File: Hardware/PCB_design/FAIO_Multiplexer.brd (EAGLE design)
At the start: 50.8 x 22.9 mm, 9 parts, among them J1 SJ1-3535NG, J2 SJ1-3535NG, J3 SJ1-3535NG, J4 SJ1-3535NG

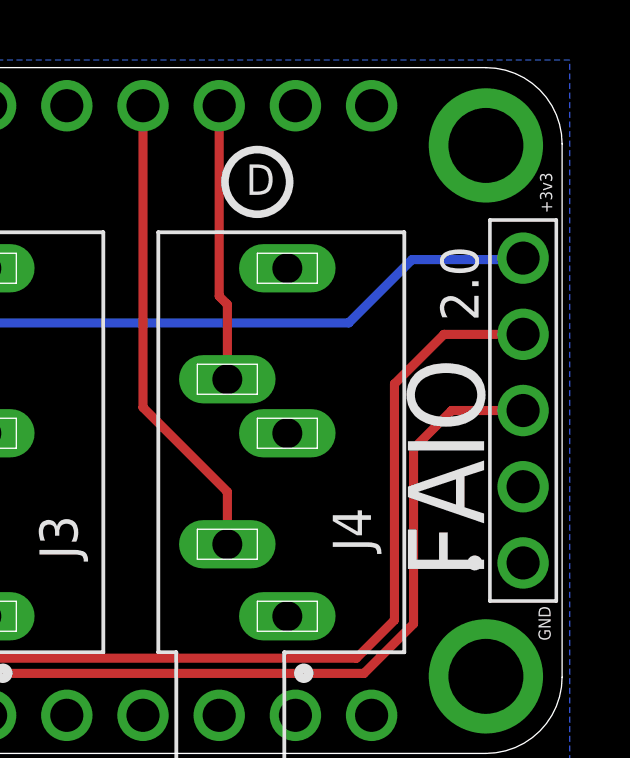
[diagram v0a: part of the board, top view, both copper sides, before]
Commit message: Updated PCB Files: 2.0 text changed to Multiplexer
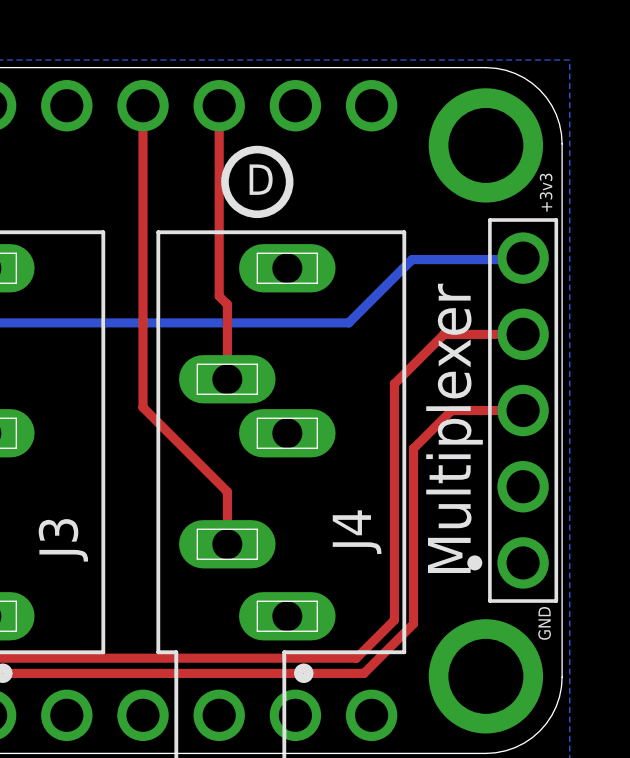
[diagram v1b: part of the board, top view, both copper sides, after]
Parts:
- renumbered U$2 to U2, U$3 to U3, U$4 to U1
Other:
- board text added: "Multiplexer"
- board text added: "https://github.com/milador/FAIO_Multiplexer"
- board text removed: "2.0"
- board text removed: "FAIO"
- board text removed: "https://github.com/milador/FAIO-2"
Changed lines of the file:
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@@
 <drawing>
 <settings>
-<setting alwaysvectorfont="no"/>
+<setting alwaysvectorfont="yes"/>
 <setting keepoldvectorfont="yes"/>
 <setting verticaltext="up"/>
@@
 <wire x1="50.8" y1="20.32" x2="50.8" y2="2.54" width="0" layer="20"/>
 <wire x1="50.8" y1="2.54" x2="48.26" y2="0" width="0" layer="20" curve="-90"/>
-<text x="48.2" y="5.842" size="2.54" layer="25" rot="R90">FAIO</text>
-<text x="48.017" y="14.412" size="1.27" layer="25" rot="R90">2.0</text>
+<text x="47.752" y="5.842" size="1.4224" layer="25" rot="R90">Multiplexer</text>
 <circle x="10.414" y="19.05" radius="1.077628125" width="0.254" layer="21"/>
 <circle x="20.574" y="19.05" radius="1.077628125" width="0.254" layer="21"/>
@@
 <text x="30.099" y="18.617" size="1.016" layer="25">C</text>
 <text x="40.259" y="18.617" size="1.016" layer="25">D</text>
-<text x="45.8978" y="18.4912" size="1.016" layer="26" rot="MR0">https://github.com/milador/FAIO-2</text>
+<text x="45.8978" y="18.4912" size="1.016" layer="26" rot="MR0">https://github.com/milador/FAIO_Multiplexer</text>
 <text x="47.244" y="8.763" size="5.08" layer="26" rot="MR0">F</text>
 <text x="37.846" y="8.763" size="5.08" layer="26" rot="MR0">A</text>
 <text x="24.892" y="8.763" size="5.08" layer="26">I</text>
 <text x="17.018" y="8.763" size="5.08" layer="26" rot="MR0">O</text>
-<text x="5.08" y="9.3032" size="2.1844" layer="26">2.0</text>
 <circle x="4.9022" y="14.5796" radius="0.14368125" width="0.3048" layer="21"/>
 <text x="50.419" y="3.7592" size="0.4064" layer="21" rot="R90">GND</text>
 <text x="50.4698" y="18.0086" size="0.4064" layer="21" rot="R90">+3v3</text>
+<text x="13.3858" y="8.2296" size="1.016" layer="26" rot="MR0">Multiplexer</text>
 </plain>
 <attributes>
@@
 <attribute name="VALUE" x="4.879" y="11.17" size="0.6096" layer="27" font="vector" ratio="20" rot="R90" align="top-center"/>
 </element>
-<element name="U$2" library="milador" library_urn="urn:adsk.eagle:library:7092934" package="CONN_1X12" package3d_urn="urn:adsk.eagle:package:6686451/2" value="CONN_1X12_FEMALECONN_1X12_FEMALE" x="44.45" y="21.59" smashed="yes" rot="MR0"/>
-<element name="U$3" library="milador" library_urn="urn:adsk.eagle:library:7092934" package="CONN_1X16" package3d_urn="urn:adsk.eagle:package:6686444/2" value="" x="6.35" y="1.27" smashed="yes" rot="MR180">
+<element name="U2" library="milador" library_urn="urn:adsk.eagle:library:7092934" package="CONN_1X12" package3d_urn="urn:adsk.eagle:package:6686451/2" value="CONN_1X12_FEMALECONN_1X12_FEMALE" x="44.45" y="21.59" smashed="yes" rot="MR0"/>
+<element name="U3" library="milador" library_urn="urn:adsk.eagle:library:7092934" package="CONN_1X16" package3d_urn="urn:adsk.eagle:package:6686444/2" value="" x="6.35" y="1.27" smashed="yes" rot="MR180">
 <attribute name="VALUE" x="6.35" y="3.175" size="1.27" layer="28" rot="MR180" align="top-center"/>
 </element>
-<element name="U$4" library="milador" library_urn="urn:adsk.eagle:library:7092934" package="CONN_1X5" package3d_urn="urn:adsk.eagle:package:6908637/1" value="CONN_1X5_MALE" x="49.5" y="6.35" smashed="yes" rot="R90"/>
+<element name="U1" library="milador" library_urn="urn:adsk.eagle:library:7092934" package="CONN_1X5" package3d_urn="urn:adsk.eagle:package:6908637/1" value="CONN_1X5_MALE" x="49.5" y="6.35" smashed="yes" rot="R90"/>
 </elements>
 <signals>
@@
 <contactref element="LED1" pad="4"/>
 <contactref element="LED1" pad="3"/>
-<contactref element="U$3" pad="4"/>
+<contactref element="U3" pad="4"/>
 <via x="2.54" y="20.2662" extent="1-16" drill="2.5" diameter="3.81"/>
 <via x="2.54" y="2.5684" extent="1-16" drill="2.5" diameter="3.81"/>
-<contactref element="U$4" pad="1"/>
+<contactref element="U1" pad="1"/>
 <contactref element="J2" pad="1"/>
 </signal>
 <signal name="+3V3">
 <contactref element="LED1" pad="2"/>
-<contactref element="U$3" pad="2"/>
+<contactref element="U3" pad="2"/>
 <wire x1="8.89" y1="1.27" x2="8.89" y2="2.54" width="0.3048" layer="1"/>
 <wire x1="5.842" y1="5.588" x2="8.89" y2="2.54" width="0.3048" layer="1"/>
-<contactref element="U$4" pad="5"/>
+<contactref element="U1" pad="5"/>
 <wire x1="49.5" y1="16.51" x2="49.3776" y2="16.4592" width="0.2032" layer="16"/>
 <wire x1="49.3776" y1="16.4592" x2="45.7962" y2="16.4592" width="0.3048" layer="16"/>
@@
 <signal name="N$5">
 <contactref element="J4" pad="3"/>
-<contactref element="U$2" pad="3"/>
+<contactref element="U2" pad="3"/>
 <wire x1="39.64" y1="12.472" x2="39.64" y2="14.97" width="0.3048" layer="1"/>
 <wire x1="39.64" y1="14.97" x2="39.37" y2="15.24" width="0.3048" layer="1"/>
@@
 </signal>
 <signal name="N$13">
-<contactref element="U$4" pad="3"/>
-<contactref element="U$3" pad="10"/>
+<contactref element="U1" pad="3"/>
+<contactref element="U3" pad="10"/>
 <wire x1="29.21" y1="1.27" x2="29.21" y2="2.159" width="0.3048" layer="1"/>
 <wire x1="44.196" y1="2.667" x2="45.847" y2="4.318" width="0.3048" layer="1"/>
@@
 </signal>
 <signal name="N$7">
-<contactref element="U$3" pad="9"/>
-<contactref element="U$4" pad="4"/>
+<contactref element="U3" pad="9"/>
+<contactref element="U1" pad="4"/>
 <wire x1="26.67" y1="1.27" x2="26.67" y2="2.032" width="0.3048" layer="1"/>
 <wire x1="43.942" y1="3.175" x2="45.212" y2="4.445" width="0.3048" layer="1"/>
@@
 </signal>
 <signal name="N$9">
-<contactref element="U$3" pad="5"/>
+<contactref element="U3" pad="5"/>
 <contactref element="J1" pad="2"/>
 <wire x1="16.51" y1="1.27" x2="16.51" y2="3.937" width="0.3048" layer="1"/>
@@
 </signal>
 <signal name="N$10">
-<contactref element="U$3" pad="6"/>
+<contactref element="U3" pad="6"/>
 <contactref element="J1" pad="3"/>
 <wire x1="9.541" y1="12.472" x2="13.436" y2="12.472" width="0.3048" layer="1"/>
@@
 <signal name="N$11">
 <contactref element="J2" pad="2"/>
-<contactref element="U$3" pad="7"/>
+<contactref element="U3" pad="7"/>
 <wire x1="19.574" y1="6.972" x2="19.574" y2="5.858" width="0.3048" layer="1"/>
 <wire x1="19.574" y1="5.858" x2="19.05" y2="5.334" width="0.3048" layer="1"/>
@@
 <signal name="N$14">
 <contactref element="J2" pad="3"/>
-<contactref element="U$3" pad="8"/>
+<contactref element="U3" pad="8"/>
 <wire x1="19.574" y1="12.472" x2="22.58" y2="12.472" width="0.3048" layer="1"/>
 <wire x1="22.58" y1="12.472" x2="24.13" y2="10.922" width="0.3048" layer="1"/>
@@
 </signal>
 <signal name="N$3">
-<contactref element="U$2" pad="4"/>
+<contactref element="U2" pad="4"/>
 <contactref element="J4" pad="2"/>
 <wire x1="36.83" y1="21.59" x2="36.83" y2="11.5316" width="0.3048" layer="1"/>
@@
 </signal>
 <signal name="N$1">
-<contactref element="U$2" pad="6"/>
+<contactref element="U2" pad="6"/>
 <contactref element="J3" pad="3"/>
 <wire x1="31.75" y1="21.59" x2="31.75" y2="19.8628" width="0.3048" layer="1"/>
@@
 <signal name="N$2">
 <contactref element="J3" pad="2"/>
-<contactref element="U$2" pad="7"/>
+<contactref element="U2" pad="7"/>
 <wire x1="29.21" y1="21.59" x2="29.21" y2="19.7866" width="0.3048" layer="1"/>
 <wire x1="29.21" y1="19.7866" x2="26.6192" y2="17.1958" width="0.3048" layer="1"/>
@@
 <signal name="N$6">
 <contactref element="R1" pad="2"/>
-<contactref element="U$2" pad="8"/>
+<contactref element="U2" pad="8"/>
 <wire x1="26.67" y1="21.59" x2="26.67" y2="20.32" width="0.3048" layer="1"/>
 <wire x1="26.67" y1="20.32" x2="26.035" y2="19.685" width="0.3048" layer="1"/>
